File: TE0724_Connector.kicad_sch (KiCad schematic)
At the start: 1 part, among them J1 SS5-80-3.50-L-D-K-TR

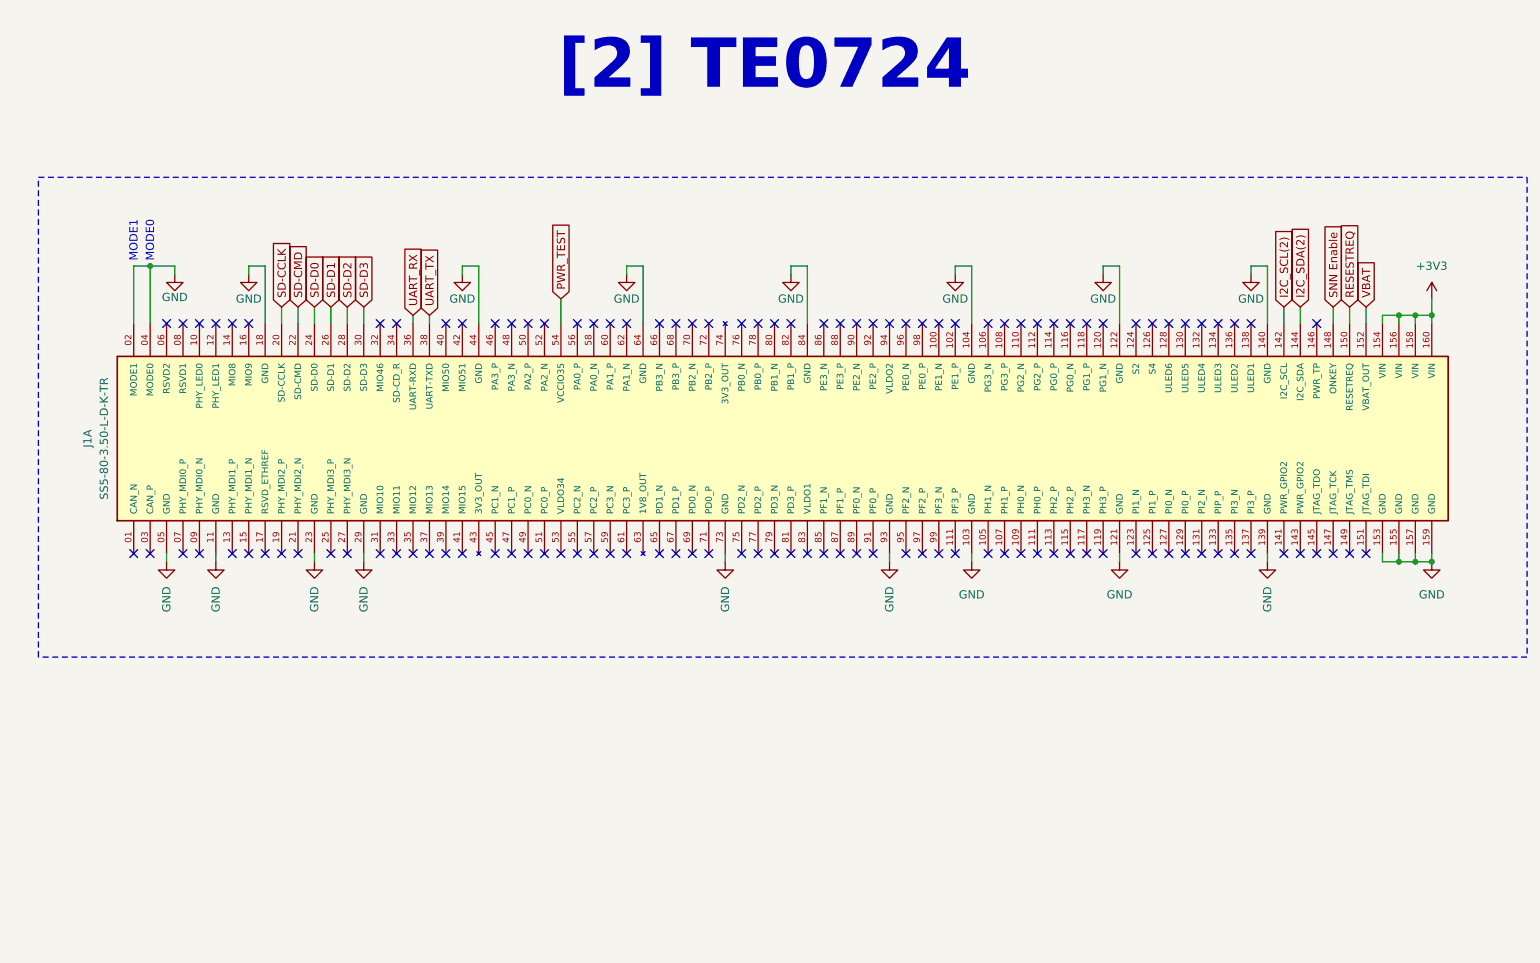
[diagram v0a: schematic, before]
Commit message: Added level shifter and breakout for ethernet
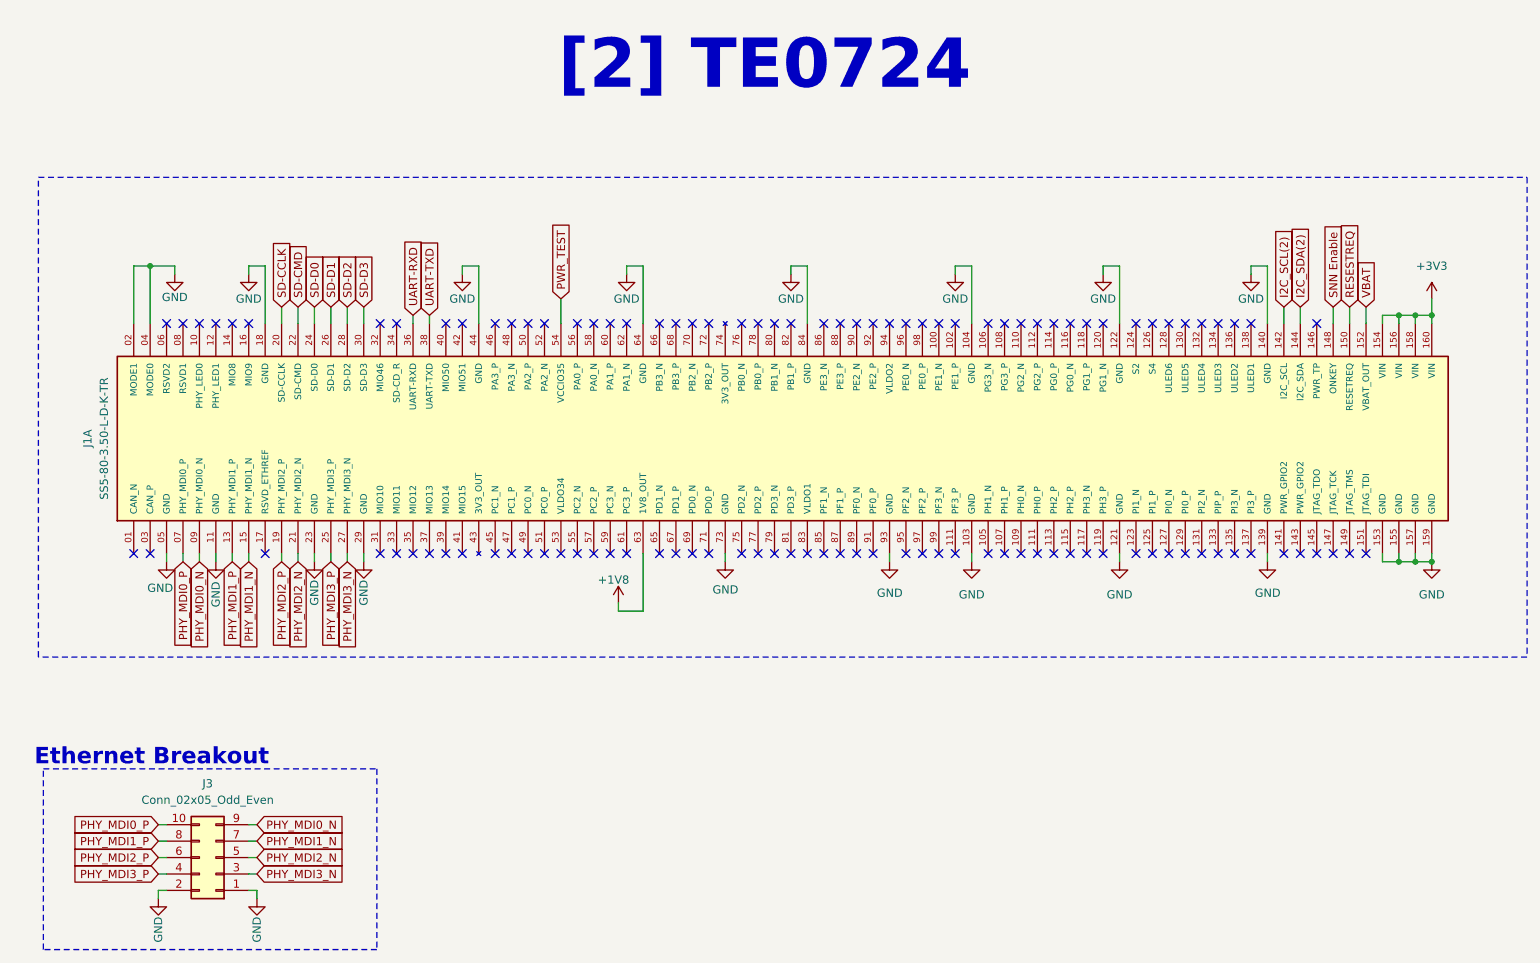
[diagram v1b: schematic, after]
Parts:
- added J3: Conn_02x05_Odd_Even, Connector_PinSocket_2.54mm:PinSocket_2x05_P2.54mm_Vertical, symbol Connector_Generic:Conn_02x05_Odd_Even
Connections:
- net GND: now also J3.1 (Pin_1), J3.2 (Pin_2)
- net PHY_MDI0_P: now reaches J1.07 (PHY_MDI0_P)
- net PHY_MDI0_P: now also J3.10 (Pin_10)
- net PHY_MDI0_N: now reaches J1.09 (PHY_MDI0_N)
- net PHY_MDI0_N: now also J3.9 (Pin_9)
- net PHY_MDI1_P: now reaches J1.13 (PHY_MDI1_P)
- net PHY_MDI1_P: now also J3.8 (Pin_8)
- net PHY_MDI1_N: now reaches J1.15 (PHY_MDI1_N)
- net PHY_MDI1_N: now also J3.7 (Pin_7)
- net PHY_MDI2_P: now reaches J1.19 (PHY_MDI2_P)
- net PHY_MDI2_P: now also J3.6 (Pin_6)
- net PHY_MDI2_N: now reaches J1.21 (PHY_MDI2_N)
- net PHY_MDI2_N: now also J3.5 (Pin_5)
- net PHY_MDI3_P: now reaches J1.25 (PHY_MDI3_P)
- net PHY_MDI3_P: now also J3.4 (Pin_4)
- net PHY_MDI3_N: now reaches J1.27 (PHY_MDI3_N)
- net PHY_MDI3_N: now also J3.3 (Pin_3)
- net +1V8: now reaches J1.63 (1V8_OUT)
- net UART_RX renamed UART-RXD
- net UART_TX renamed UART-TXD
- no-connect marks 117 -> 109
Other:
- note added: "Ethernet Breakout"
- note removed: "MODE0"
- note removed: "MODE1"
